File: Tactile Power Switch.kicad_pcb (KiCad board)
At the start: 2 copper layers, 24 x 30 mm, 16 parts, among them J1 OSTTC020162, J2 OSTTC020162, Q1 BC847B_215, Q2 BC847B_215, Q4 NDT2955

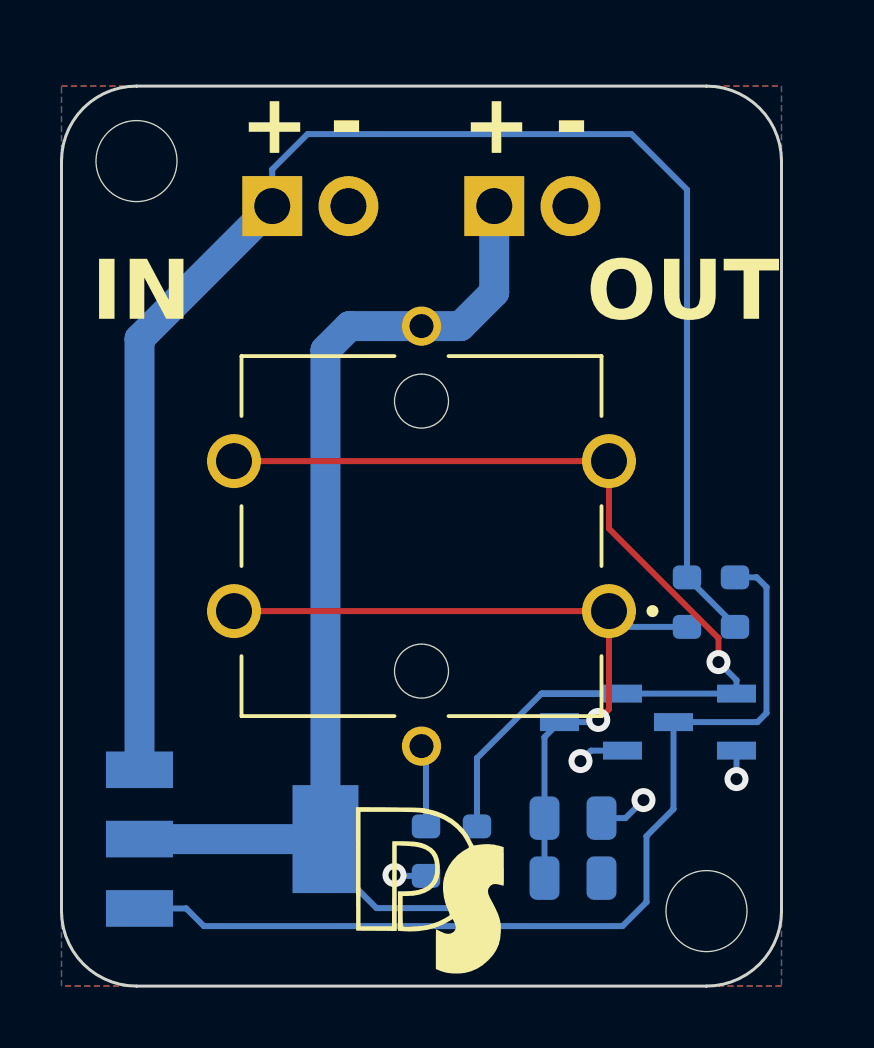
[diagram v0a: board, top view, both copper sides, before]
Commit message: MOSFET footprint update, Silkscreen update
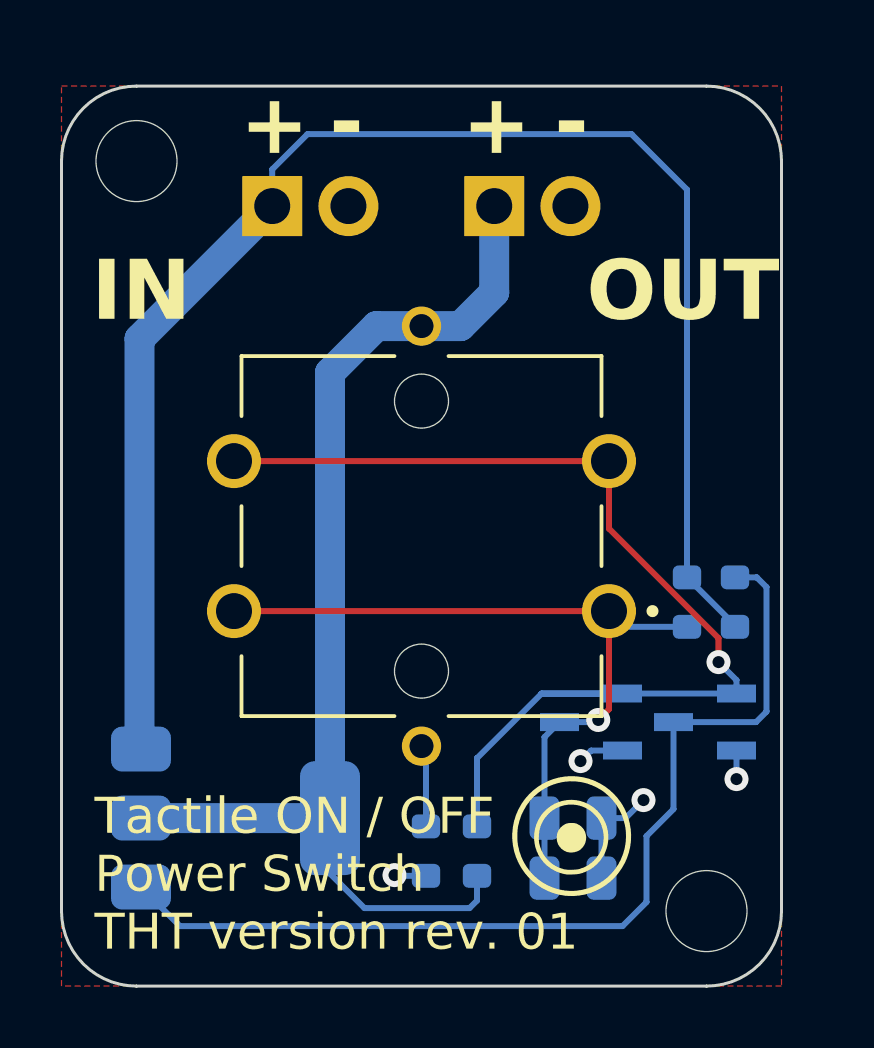
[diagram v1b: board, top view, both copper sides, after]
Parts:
- G***: moved to F.Cu
- G***: moved to B.Cu
- Q4: footprint MOSFET:SOT223 -> Package_TO_SOT_SMD:SOT-223
- moved G*** 11.8 mm to (120.2, 59.0), turned to 180 degrees
- moved G*** 11.2 mm to (125.0, 69.0), turned to 0 degrees
- moved Q4 0.71 mm to (113.8, 68.4), turned to 0 degrees
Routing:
- net GND: track 5.20 -> 7.20 mm
- net +12V: track 52.2 -> 51.5 mm
- removed copper zone on B.Cu, net GND
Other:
- board text added: "Tactile ON / OFF Power Switch THT version rev. 01"
